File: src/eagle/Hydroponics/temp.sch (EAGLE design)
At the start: 2 parts

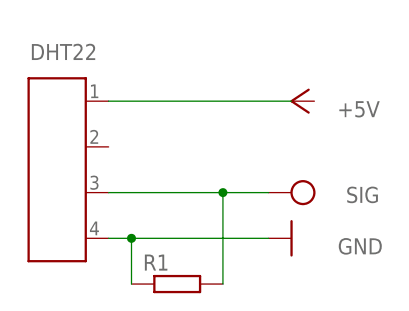
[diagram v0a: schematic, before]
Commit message: change dht schema
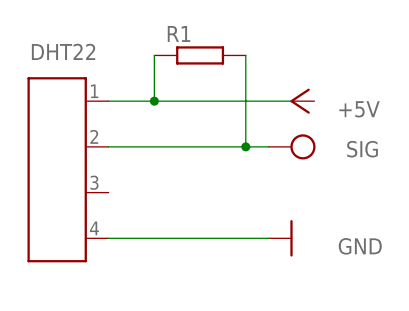
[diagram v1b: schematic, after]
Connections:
- net GND: no longer R1.1
- net N$1: now also R1.1
- net VSS: now also DHT22.2; no longer DHT22.3
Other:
- moved on the sheet: R1
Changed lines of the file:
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@@
 </plain>
 <instances>
-<instance part="R1" gate="G$1" x="-7.62" y="93.98">
-<attribute name="OC_NEWARK" x="-7.62" y="93.98" size="1.778" layer="96" rot="R180" display="off"/>
-<attribute name="MF" x="-7.62" y="93.98" size="1.778" layer="96" rot="R180" display="off"/>
-<attribute name="MPN" x="-7.62" y="93.98" size="1.778" layer="96" rot="R180" display="off"/>
+<instance part="R1" gate="G$1" x="-5.08" y="119.38">
+<attribute name="OC_NEWARK" x="-5.08" y="119.38" size="1.778" layer="96" rot="R180" display="off"/>
+<attribute name="MF" x="-5.08" y="119.38" size="1.778" layer="96" rot="R180" display="off"/>
+<attribute name="MPN" x="-5.08" y="119.38" size="1.778" layer="96" rot="R180" display="off"/>
 </instance>
 <instance part="DHT22" gate="G$1" x="-20.32" y="109.22" smashed="yes" rot="R270">
@@
 <attribute name="HERSTELLER" x="-24.13" y="118.11" size="1.778" layer="96" rot="R90"/>
 </instance>
-<instance part="SUPPLY1" gate="G$1" x="5.08" y="104.14" smashed="yes" rot="R90">
-<attribute name="VALUE" x="14.859" y="104.775" size="1.778" layer="96" rot="R180"/>
+<instance part="SUPPLY1" gate="G$1" x="5.08" y="109.22" smashed="yes" rot="R90">
+<attribute name="VALUE" x="14.859" y="109.855" size="1.778" layer="96" rot="R180"/>
 </instance>
 <instance part="GND1" gate="1" x="5.08" y="99.06" smashed="yes" rot="R90">
@@
 </busses>
 <nets>
-<net name="VSS" class="0">
-<segment>
-<pinref part="SUPPLY1" gate="G$1" pin="VSS"/>
-<pinref part="DHT22" gate="G$1" pin="3"/>
-<wire x1="-15.24" y1="104.14" x2="-2.54" y2="104.14" width="0.1524" layer="91"/>
-<pinref part="R1" gate="G$1" pin="2"/>
-<wire x1="-2.54" y1="104.14" x2="2.54" y2="104.14" width="0.1524" layer="91"/>
-<wire x1="-2.54" y1="93.98" x2="-2.54" y2="104.14" width="0.1524" layer="91"/>
-<junction x="-2.54" y="104.14"/>
-</segment>
-</net>
 <net name="GND" class="0">
 <segment>
 <pinref part="DHT22" gate="G$1" pin="4"/>
-<wire x1="-15.24" y1="99.06" x2="-12.7" y2="99.06" width="0.1524" layer="91"/>
-<pinref part="R1" gate="G$1" pin="1"/>
-<wire x1="-12.7" y1="99.06" x2="2.54" y2="99.06" width="0.1524" layer="91"/>
-<wire x1="-12.7" y1="93.98" x2="-12.7" y2="99.06" width="0.1524" layer="91"/>
+<wire x1="-15.24" y1="99.06" x2="2.54" y2="99.06" width="0.1524" layer="91"/>
 <pinref part="GND1" gate="1" pin="GND"/>
-<junction x="-12.7" y="99.06"/>
 </segment>
 </net>
@@
 <segment>
 <pinref part="DHT22" gate="G$1" pin="1"/>
-<wire x1="-15.24" y1="114.3" x2="5.08" y2="114.3" width="0.1524" layer="91"/>
+<wire x1="-15.24" y1="114.3" x2="-10.16" y2="114.3" width="0.1524" layer="91"/>
+<pinref part="R1" gate="G$1" pin="1"/>
+<wire x1="-10.16" y1="114.3" x2="5.08" y2="114.3" width="0.1524" layer="91"/>
+<wire x1="-10.16" y1="119.38" x2="-10.16" y2="114.3" width="0.1524" layer="91"/>
+<junction x="-10.16" y="114.3"/>
 </segment>
 </net>
+<net name="VSS" class="0">
+<segment>
+<pinref part="DHT22" gate="G$1" pin="2"/>
+<pinref part="SUPPLY1" gate="G$1" pin="VSS"/>
+<wire x1="-15.24" y1="109.22" x2="0" y2="109.22" width="0.1524" layer="91"/>
+<pinref part="R1" gate="G$1" pin="2"/>
+<wire x1="0" y1="109.22" x2="2.54" y2="109.22" width="0.1524" layer="91"/>
+<wire x1="0" y1="119.38" x2="0" y2="109.22" width="0.1524" layer="91"/>
+<junction x="0" y="109.22"/>
+</segment>
+</net>
